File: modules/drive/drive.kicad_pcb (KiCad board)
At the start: 2 copper layers, 30.5 x 68.6 mm, 21 parts, among them U1 MCP6002-xSN

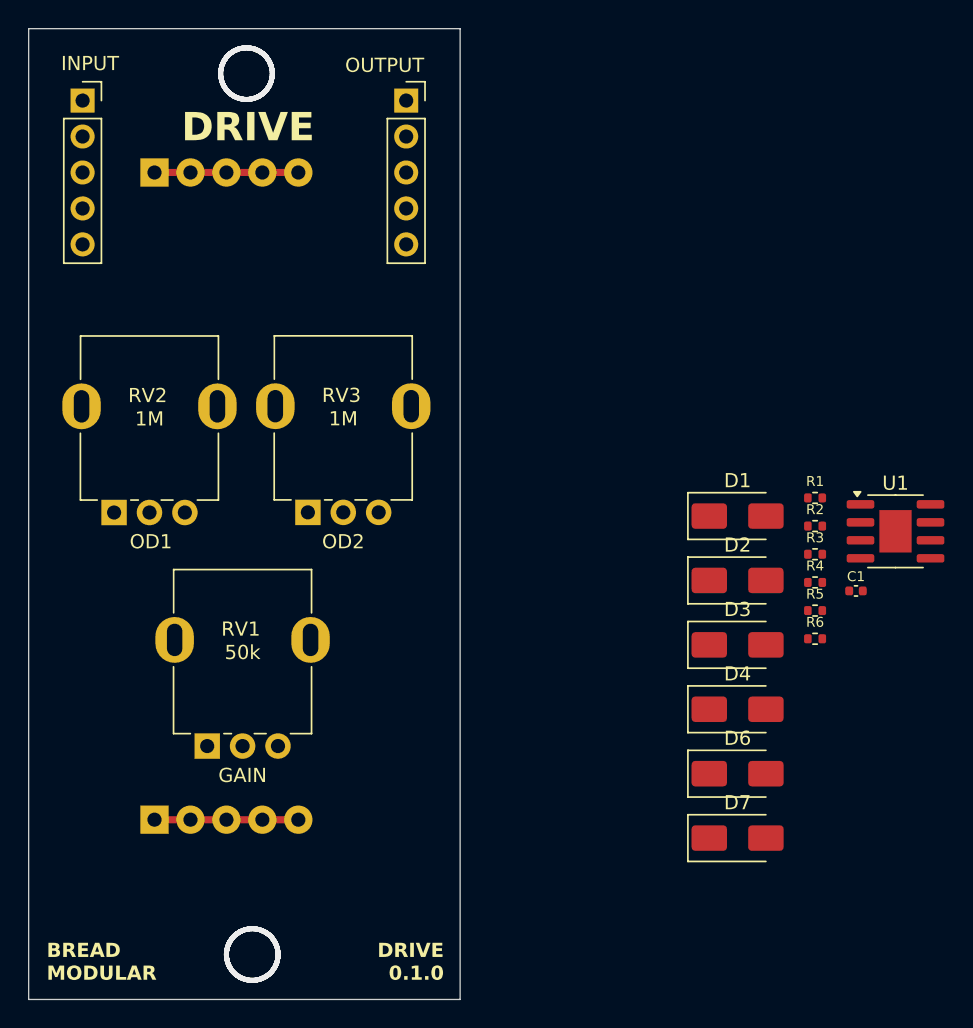
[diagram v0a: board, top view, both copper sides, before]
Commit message: drive: finished pcb routing
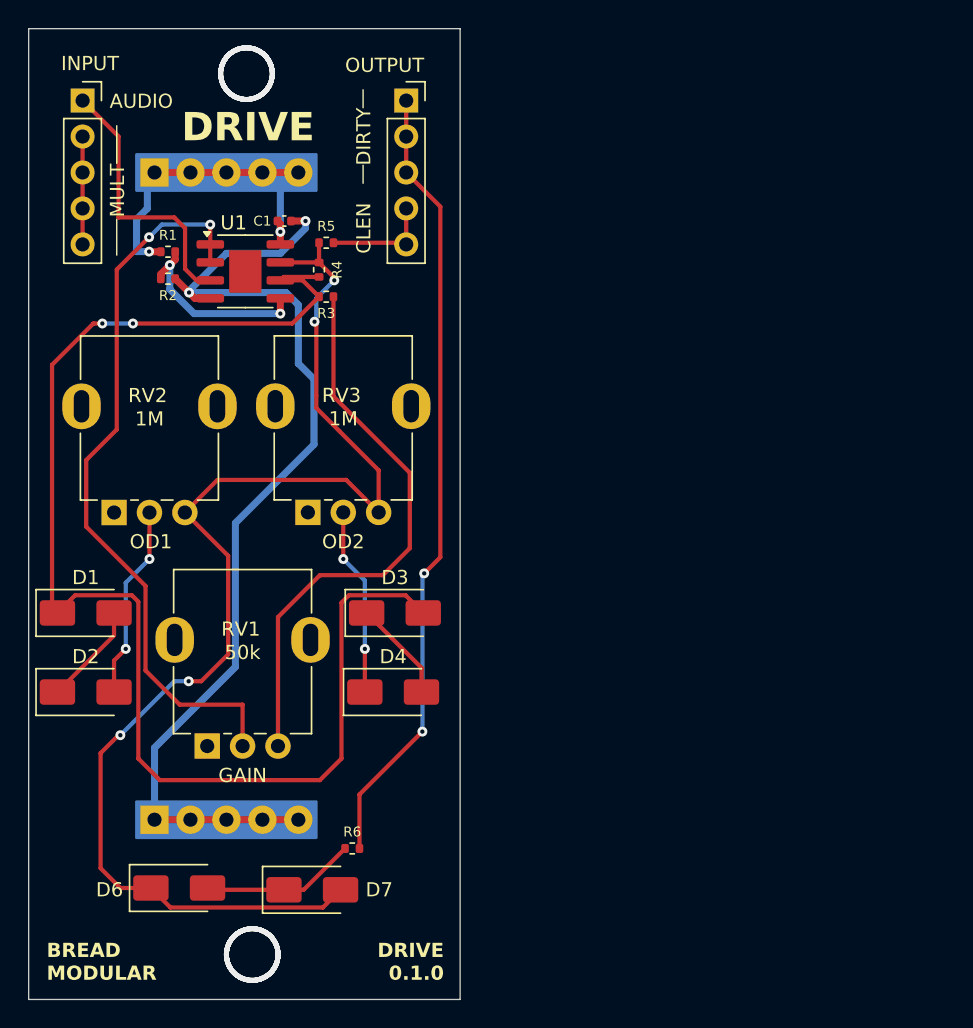
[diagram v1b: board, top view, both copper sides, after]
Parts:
- moved U1 49.5 mm to (62.3, 57.8)
- moved R2 48.9 mm to (56.8, 58.3)
- moved R1 48.9 mm to (56.8, 56.4)
- moved C1 48.1 mm to (65.1, 54.2)
- moved D2 46.7 mm to (51.0, 87.5)
- moved D1 46.6 mm to (51.0, 81.9)
- moved R5 43.2 mm to (68.0, 55.8)
- moved R4 41.4 mm to (67.5, 57.7), turned to 90 degrees
- moved D6 40.3 mm to (57.6, 101.3)
- moved R3 39.0 mm to (68.0, 59.6), turned to 180 degrees
- moved R6 35.9 mm to (69.8, 98.6)
- moved D7 30.3 mm to (67.0, 101.5)
- moved D4 24.4 mm to (72.7, 87.5)
- moved D3 24.3 mm to (72.9, 81.9)
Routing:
- net Net-(D1-K): track 0.00 -> 95.2 mm, vias 0 -> 2
- net Net-(D6-K): track 0.00 -> 90.2 mm, vias 0 -> 4
- net GND: track 10.2 -> 74.5 mm, vias 0 -> 2
- net AUDIO_OUT_DIRTY: track 0.00 -> 56.2 mm, vias 0 -> 2
- net Net-(U1A--): track 0.00 -> 52.3 mm, vias 0 -> 2
- net Net-(R3-Pad1): track 0.00 -> 40.4 mm
- net AUDIO_IN: track 0.00 -> 19.3 mm
- net V_SUPPLY: track 10.2 -> 24.4 mm, vias 0 -> 2
- net Net-(D2-A): track 0.00 -> 13.7 mm, vias 0 -> 2
- net V_MID: track 0.00 -> 13.6 mm, vias 0 -> 2
- net Net-(D4-K): track 0.00 -> 13.3 mm, vias 0 -> 2
- net Net-(D6-A): track 0.00 -> 11.0 mm
- net AUDIO_OUT_CLEAN: track 0.00 -> 7.73 mm
- net Net-(INPUT1-Pin_2): track 0.00 -> 7.62 mm
- net Net-(D1-A): track 0.00 -> 7.24 mm
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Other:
- board text added: "AUDIO"
- board text added: "CLEN"
- board text added: "DIRTY"
- board text added: "MULT"

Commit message: drive: Remove radio freq. capturing with the gain. This is due to the high-gain nature & the use of non-inverting buffer. Now change it to an inverting buffer & all is gone.
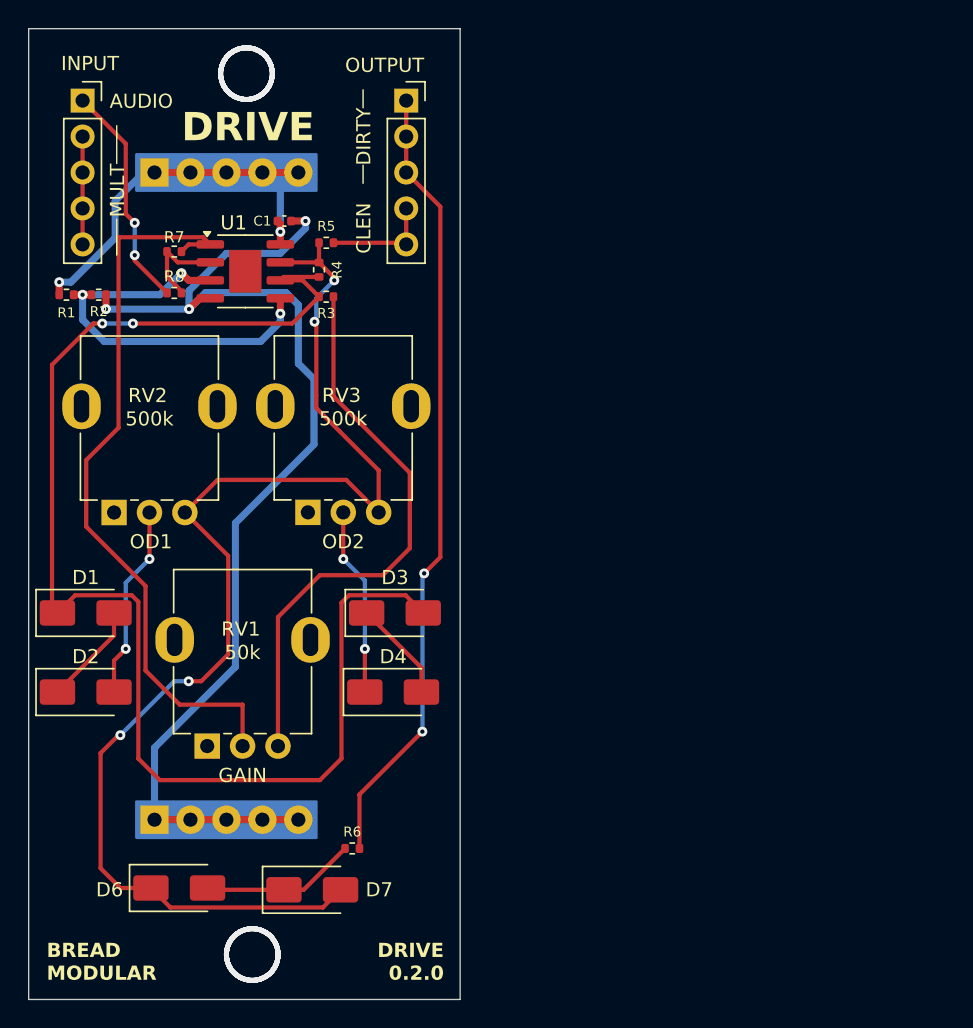
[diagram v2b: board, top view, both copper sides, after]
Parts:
- added R7: 100k, Resistor_SMD:R_0402_1005Metric, F.Cu at (57.3, 56.4)
- added R8: 100k, Resistor_SMD:R_0402_1005Metric, F.Cu at (57.3, 59.3)
- RV2, RV3: value 1M -> 500k
- moved R1 7.79 mm to (49.7, 59.4)
- moved R2 5.02 mm to (51.9, 59.4)
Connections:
- RV1 pad 2: Net-(U1A--) -> Net-(R7-Pad2)
- U1 pad 1: Net-(U1A--) -> Net-(R7-Pad2)
- U1 pad 3: AUDIO_IN -> V_MID
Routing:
- net Net-(R7-Pad2): track 0.00 -> 53.0 mm
- net Net-(U1A--): track 52.3 -> 6.71 mm, vias 2 -> 0
- net V_MID: track 13.6 -> 29.7 mm, vias 2 -> 3
- net GND: track 74.5 -> 81.8 mm, vias 2 -> 3
- net V_SUPPLY: track 24.4 -> 29.0 mm
- net AUDIO_IN: track 19.3 -> 16.1 mm, vias 0 -> 2
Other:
- board text added: "DRIVE 0.2.0"
- board text removed: "DRIVE 0.1.0"
